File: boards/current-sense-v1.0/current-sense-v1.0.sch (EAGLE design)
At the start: 89 parts, among them IC1 ISO7241, IC2 ISO7241, IC3 ISO7242, IC4 ISO7240, J1 4-PIN_2MM-H, J2 MKS-1658, J3 8-PIN_2MM-H, J6 DF22-2, Q1 IRFH7545, Q2 IRFH7545, Q3 IRFH7545, Q4 IRFH7545, Q5 IRFH7545, Q6 IRFH7545, U1 DRV8303DCA, U13 TLV70233DBVR, U2 INA240PWR, U3 INA240PWR, U4 INA240PWR, U6 ADS8028IRTJT, U7 MPM3620GQV-P, U8 VND5E006ASPTR-E, U9 TLV70433

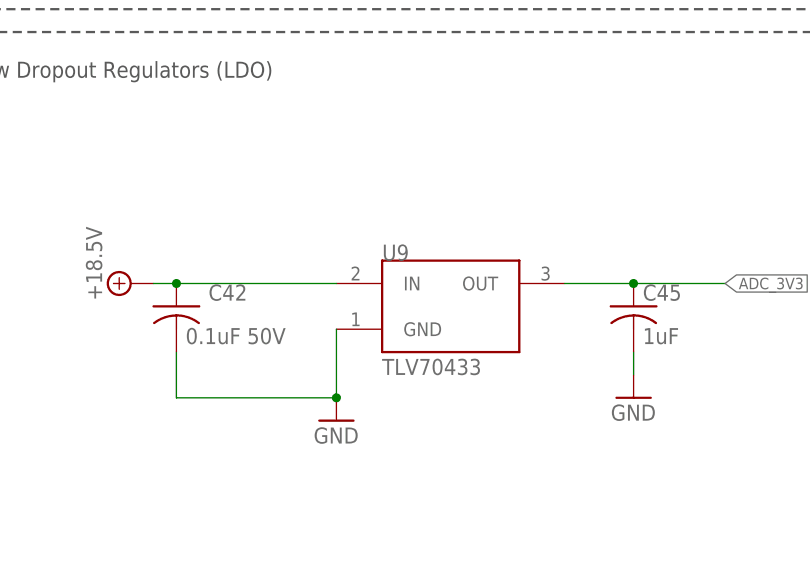
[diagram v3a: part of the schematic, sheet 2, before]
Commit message: Revert "fixed U9 LDO connections"
This reverts commit 927cff76196117dea27b8f474de1fa187c808058.
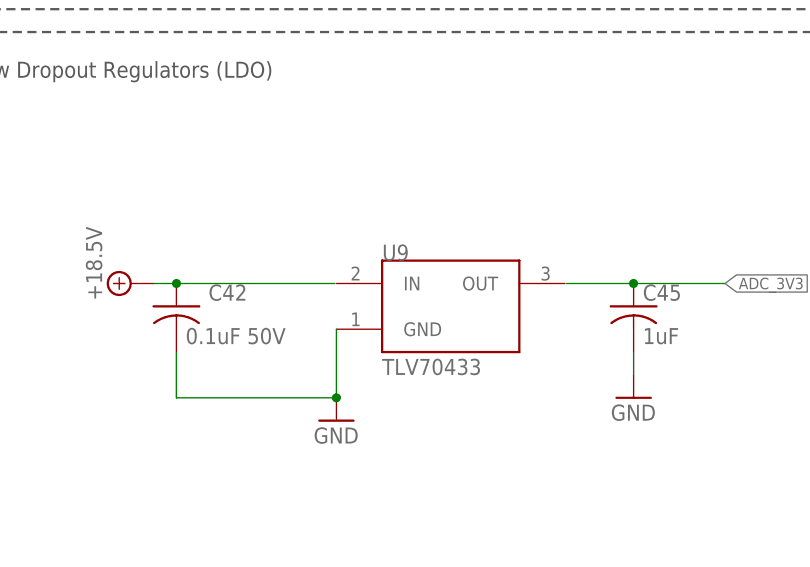
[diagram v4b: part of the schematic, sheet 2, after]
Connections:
- net +18.5V: no longer U9.IN
- net ADC_3V3: no longer U9.OUT
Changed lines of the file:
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@@
 <pinref part="C42" gate="G$1" pin="1"/>
 <wire x1="190.5" y1="96.52" x2="187.96" y2="96.52" width="0.1524" layer="91"/>
+<junction x="190.5" y="96.52"/>
 <pinref part="SUPPLY42" gate="G$1" pin="+18.5V"/>
-<pinref part="U9" gate="G$1" pin="IN"/>
-<wire x1="190.5" y1="96.52" x2="208.28" y2="96.52" width="0.1524" layer="91"/>
-<junction x="190.5" y="96.52"/>
+<wire x1="208.1276" y1="96.52" x2="190.5" y2="96.52" width="0.1524" layer="91"/>
 </segment>
 </net>
@@
 <segment>
 <pinref part="C45" gate="G$1" pin="1"/>
+<junction x="241.3" y="96.52"/>
 <wire x1="241.3" y1="96.52" x2="251.46" y2="96.52" width="0.1524" layer="91"/>
 <label x="251.46" y="96.52" size="1.27" layer="95" xref="yes"/>
-<pinref part="U9" gate="G$1" pin="OUT"/>
-<wire x1="233.68" y1="96.52" x2="241.3" y2="96.52" width="0.1524" layer="91"/>
-<junction x="241.3" y="96.52"/>
+<wire x1="233.8324" y1="96.52" x2="241.3" y2="96.52" width="0.1524" layer="91"/>
 </segment>
 </net>

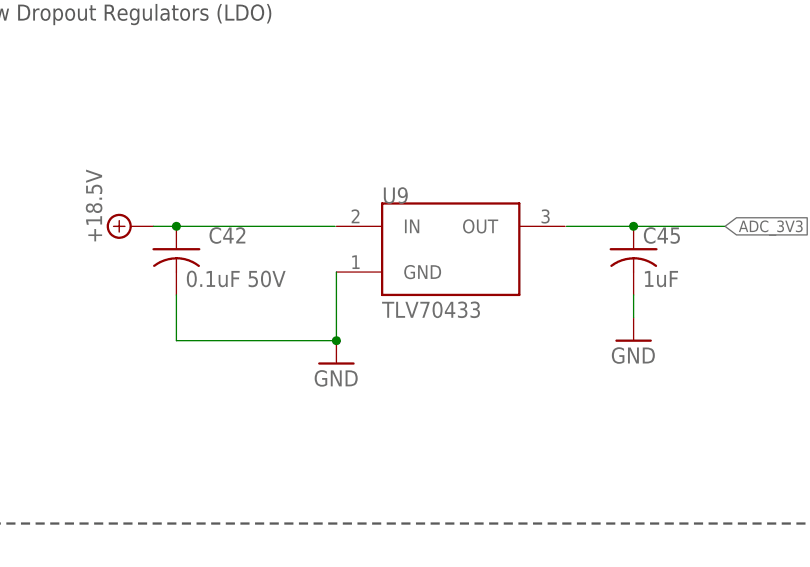
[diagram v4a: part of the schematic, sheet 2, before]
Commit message: fixed 3V3 connection on LDO
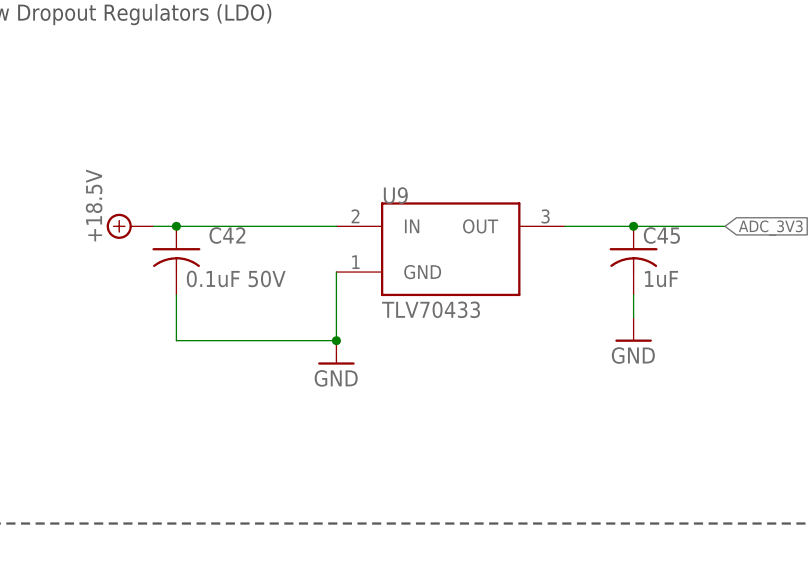
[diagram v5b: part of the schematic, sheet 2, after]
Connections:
- net +18.5V: now also U9.IN
- net ADC_3V3: now also U9.OUT
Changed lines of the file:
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@@
 <wire x1="190.5" y1="88.9" x2="190.5" y2="83.82" width="0.1524" layer="91"/>
 <wire x1="190.5" y1="83.82" x2="208.28" y2="83.82" width="0.1524" layer="91"/>
+<pinref part="GND75" gate="1" pin="GND"/>
 <pinref part="U9" gate="G$1" pin="GND"/>
-<wire x1="208.28" y1="83.82" x2="208.28" y2="91.44" width="0.1524" layer="91"/>
-<pinref part="GND75" gate="1" pin="GND"/>
+<wire x1="208.28" y1="91.44" x2="208.28" y2="83.82" width="0.1524" layer="91"/>
 <junction x="208.28" y="83.82"/>
 </segment>
@@
 <pinref part="C42" gate="G$1" pin="1"/>
 <wire x1="190.5" y1="96.52" x2="187.96" y2="96.52" width="0.1524" layer="91"/>
+<pinref part="SUPPLY42" gate="G$1" pin="+18.5V"/>
+<pinref part="U9" gate="G$1" pin="IN"/>
+<wire x1="190.5" y1="96.52" x2="208.28" y2="96.52" width="0.1524" layer="91"/>
 <junction x="190.5" y="96.52"/>
-<pinref part="SUPPLY42" gate="G$1" pin="+18.5V"/>
-<wire x1="208.1276" y1="96.52" x2="190.5" y2="96.52" width="0.1524" layer="91"/>
 </segment>
 </net>
@@
 <segment>
 <pinref part="C45" gate="G$1" pin="1"/>
-<junction x="241.3" y="96.52"/>
 <wire x1="241.3" y1="96.52" x2="251.46" y2="96.52" width="0.1524" layer="91"/>
 <label x="251.46" y="96.52" size="1.27" layer="95" xref="yes"/>
-<wire x1="233.8324" y1="96.52" x2="241.3" y2="96.52" width="0.1524" layer="91"/>
-</segment>
-</net>
+<pinref part="U9" gate="G$1" pin="OUT"/>
+<wire x1="233.68" y1="96.52" x2="241.3" y2="96.52" width="0.1524" layer="91"/>
+<junction x="241.3" y="96.52"/>
+</segment>
+</net>

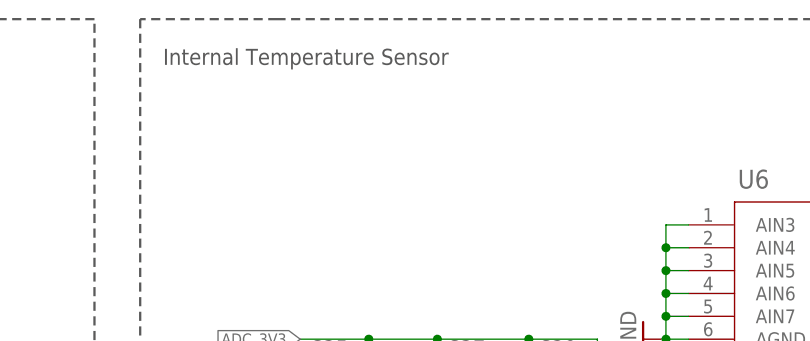
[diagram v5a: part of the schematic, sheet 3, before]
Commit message: changed name of U6 border
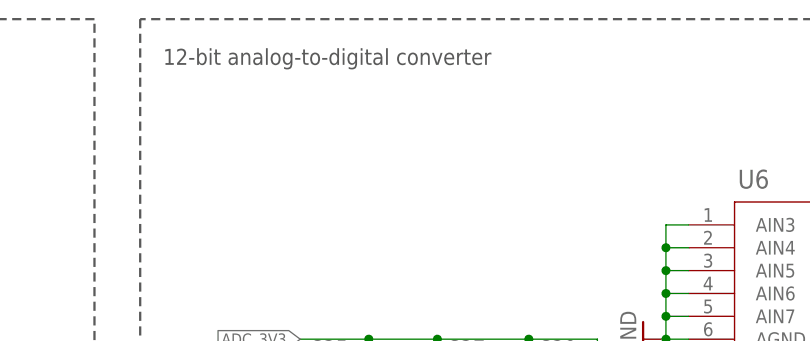
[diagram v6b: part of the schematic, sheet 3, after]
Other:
- note added: "12-bit analog-to-digital converter"
- note removed: "Internal Temperature Sensor"
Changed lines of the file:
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@@
 <wire x1="127" y1="43.18" x2="127" y2="63.5" width="0.254" layer="97" style="shortdash"/>
 <text x="20.32" y="193.04" size="1.778" layer="97">Digital Isolators</text>
-<text x="129.54" y="193.04" size="1.778" layer="97">Internal Temperature Sensor</text>
+<text x="129.54" y="193.04" size="1.778" layer="97">12-bit analog-to-digital converter</text>
 </plain>
 <instances>
